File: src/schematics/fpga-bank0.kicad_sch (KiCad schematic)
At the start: 1 part

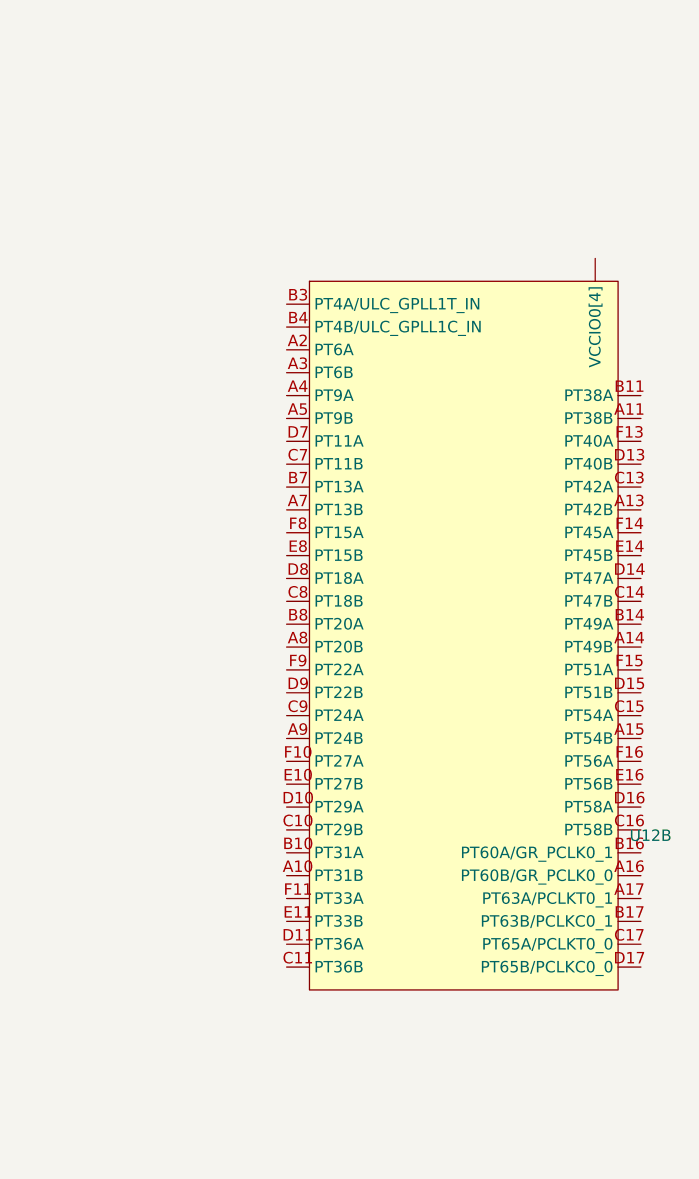
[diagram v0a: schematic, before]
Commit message: Draft connections between the FPGA and the memories
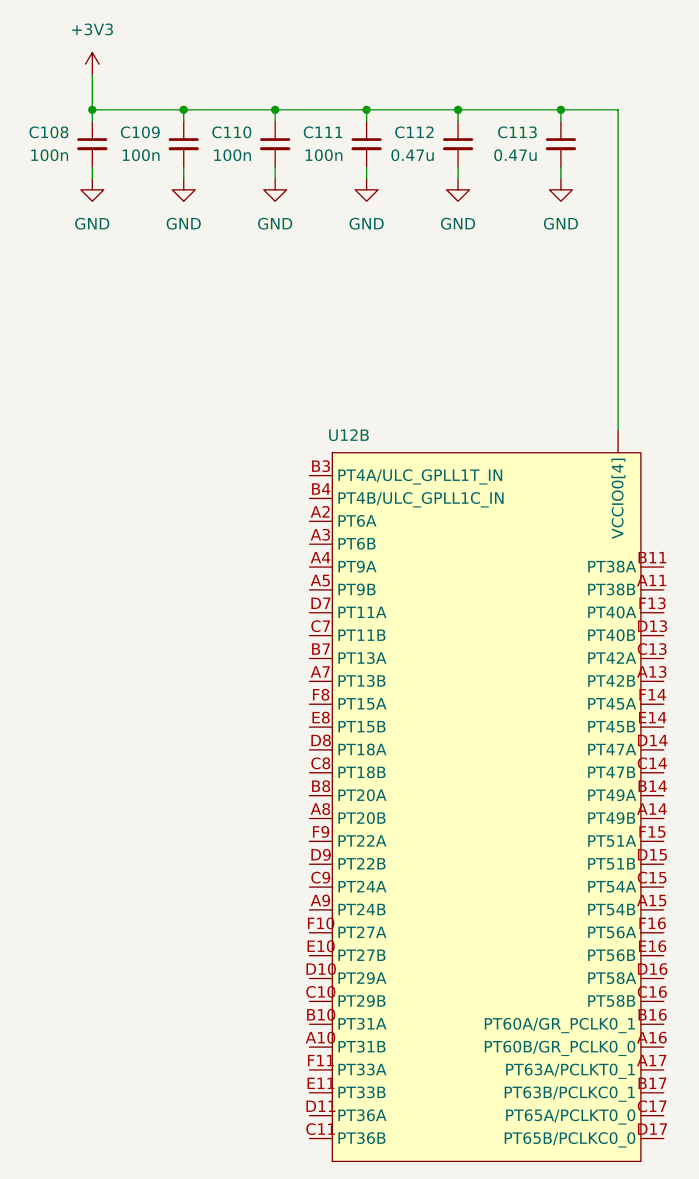
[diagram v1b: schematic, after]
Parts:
- added C108, C109, C110, C111: 100n, symbol Device:C_Small
- added C112, C113: 0.47u, symbol Device:C_Small
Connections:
- net VCCIO0 renamed +3V3
- net +3V3: now also C108.1, C109.1, C110.1, C111.1, C112.1, C113.1
- new net GND: C108.2, C109.2, C110.2, C111.2, C112.2, C113.2
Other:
- moved on the sheet: U12B

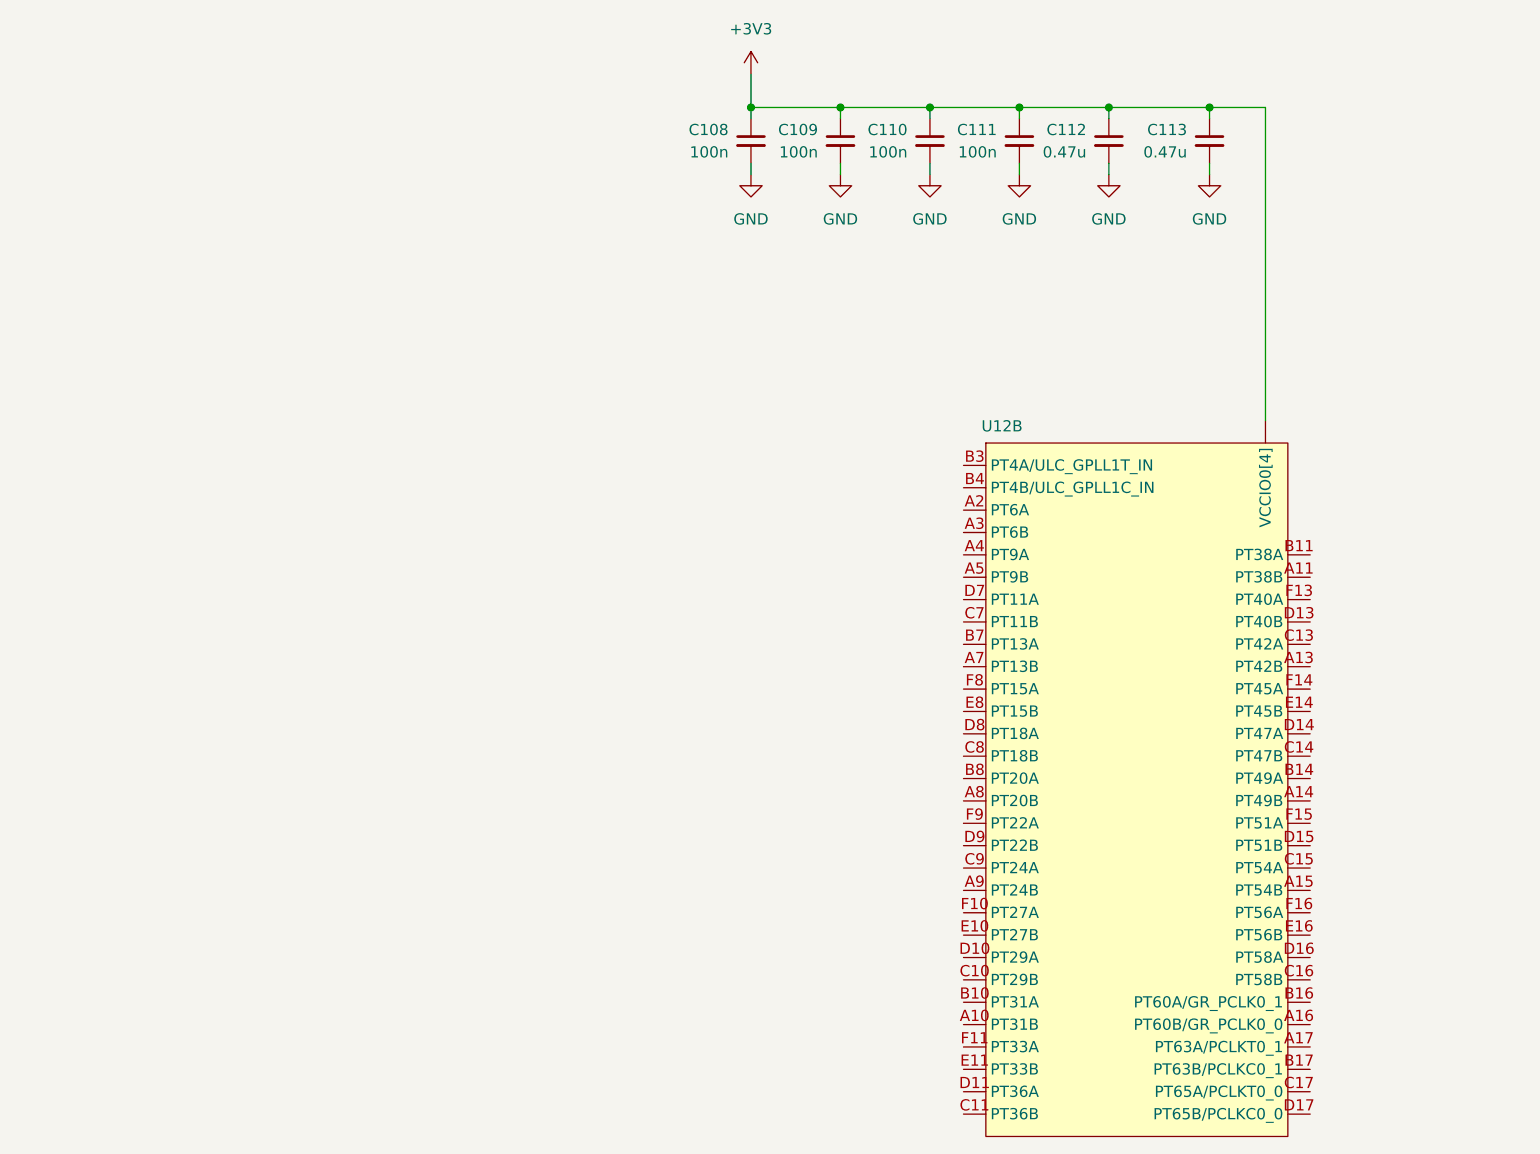
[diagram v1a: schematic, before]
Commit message: Adds draft of IO connector schematic connections to FPGA
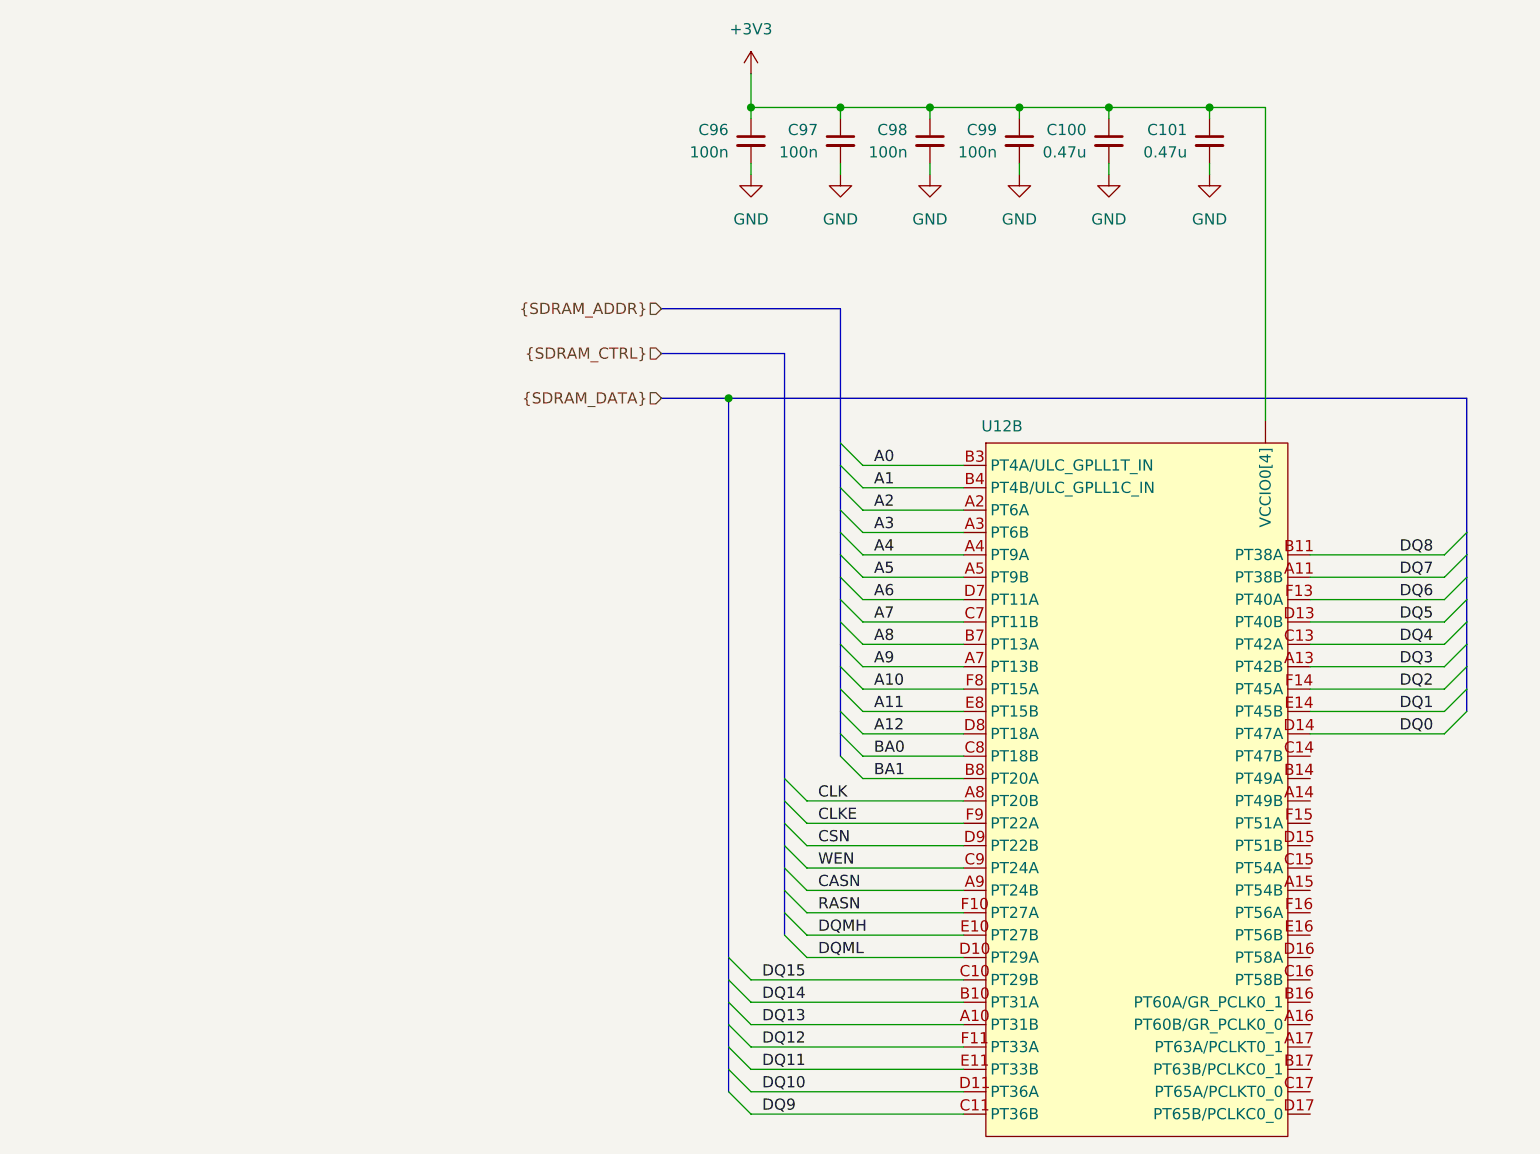
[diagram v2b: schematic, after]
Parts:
- removed C108, C109, C110, C111: 100n, symbol Device:C_Small
- removed C112, C113: 0.47u, symbol Device:C_Small
- added C100, C101: 0.47u, symbol Device:C_Small
- added C96, C97, C98, C99: 100n, symbol Device:C_Small
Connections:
- net +3V3: now also C100.1, C101.1, C96.1, C97.1, C98.1, C99.1
- net GND: now also C100.2, C101.2, C96.2, C97.2, C98.2, C99.2
- net DQ13: now reaches U12.A10 (PT31B)
- net DQ7: now reaches U12.A11 (PT38B)
- net DQ3: now reaches U12.A13 (PT42B)
- net A2: now reaches U12.A2 (PT6A)
- net A3: now reaches U12.A3 (PT6B)
- net A4: now reaches U12.A4 (PT9A)
- net A5: now reaches U12.A5 (PT9B)
- net A9: now reaches U12.A7 (PT13B)
- net CLK: now reaches U12.A8 (PT20B)
- net CASN: now reaches U12.A9 (PT24B)
- net DQ14: now reaches U12.B10 (PT31A)
- net DQ8: now reaches U12.B11 (PT38A)
- net A0: now reaches U12.B3 (PT4A/ULC_GPLL1T_IN)
- net A1: now reaches U12.B4 (PT4B/ULC_GPLL1C_IN)
- net A8: now reaches U12.B7 (PT13A)
- net BA1: now reaches U12.B8 (PT20A)
- net DQ15: now reaches U12.C10 (PT29B)
- net DQ9: now reaches U12.C11 (PT36B)
- net DQ4: now reaches U12.C13 (PT42A)
- net A7: now reaches U12.C7 (PT11B)
- net BA0: now reaches U12.C8 (PT18B)
- net WEN: now reaches U12.C9 (PT24A)
- net DQML: now reaches U12.D10 (PT29A)
- net DQ10: now reaches U12.D11 (PT36A)
- net DQ5: now reaches U12.D13 (PT40B)
- net DQ0: now reaches U12.D14 (PT47A)
- net A6: now reaches U12.D7 (PT11A)
- net A12: now reaches U12.D8 (PT18A)
- net CSN: now reaches U12.D9 (PT22B)
- net DQMH: now reaches U12.E10 (PT27B)
- net DQ11: now reaches U12.E11 (PT33B)
- net DQ1: now reaches U12.E14 (PT45B)
- net A11: now reaches U12.E8 (PT15B)
- net RASN: now reaches U12.F10 (PT27A)
- net DQ12: now reaches U12.F11 (PT33A)
- net DQ6: now reaches U12.F13 (PT40A)
- net DQ2: now reaches U12.F14 (PT45A)
- net A10: now reaches U12.F8 (PT15A)
- net CLKE: now reaches U12.F9 (PT22A)
